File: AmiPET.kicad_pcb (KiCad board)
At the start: 2 copper layers, 68.6 x 53.3 mm, 11 parts, among them J1 Power, J2 Digital/PWM, J3 Analog, J4 Digital/PWM, J6 PET Keyboard Connector, J7 AMIGA Keyboard Connector, U1 M3493B2

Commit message: PCB Project update
tweaked layout
new 3d models
added schematic, production files, bom and image
removed old painted schematic
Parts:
- added C1: C, Capacitor_THT:C_Disc_D6.0mm_W2.5mm_P5.00mm, F.Cu at (81.6, 52.1)
- J1, J4: footprint Connector_PinSocket_2.54mm:PinSocket_1x08_P2.54mm_Vertical -> AmiPet_lib_fp:PinSocket_1x08_P2.54mm_Vertical
- J2: footprint Connector_PinSocket_2.54mm:PinSocket_1x10_P2.54mm_Vertical -> AmiPet_lib_fp:PinSocket_1x10_P2.54mm_Vertical
- J3: footprint Connector_PinSocket_2.54mm:PinSocket_1x06_P2.54mm_Vertical -> AmiPet_lib_fp:PinSocket_1x06_P2.54mm_Vertical
- MH1, MH2, MH3, MH4: footprint Arduino_MountingHole:MountingHole_3.2mm -> AmiPet_lib_fp:MountingHole_3.2mm
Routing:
- net VCC: track 84.9 -> 82.9 mm
- net /Y0: track 40.5 -> 39.2 mm
- net /KCLK: track 48.7 -> 47.6 mm, vias 2 -> 0
- net /X7: track 24.5 -> 23.8 mm
- net /AY2: track 55.5 -> 56.1 mm
- net /Y3: track 14.0 -> 13.3 mm
- net /X9: track 24.5 -> 23.8 mm
- net /X8: track 24.5 -> 23.8 mm
- net /X6: track 24.5 -> 23.8 mm
- net /AX3: track 58.6 -> 57.9 mm
- net /KDAT: track 56.4 -> 56.3 mm, vias 2 -> 0
- net GND: vias 8 -> 6
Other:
- outline, holes or cut-outs redrawn
- board text added: "CLK"
- board text added: "DAT"
- board text added: "M3493B2"
- board text added: "X3"
- board text added: "_{AMI}"
- board text removed: "C3"
- board text removed: "KCLK"
- board text removed: "KDAT"
- board text removed: "_{AMI}PET"

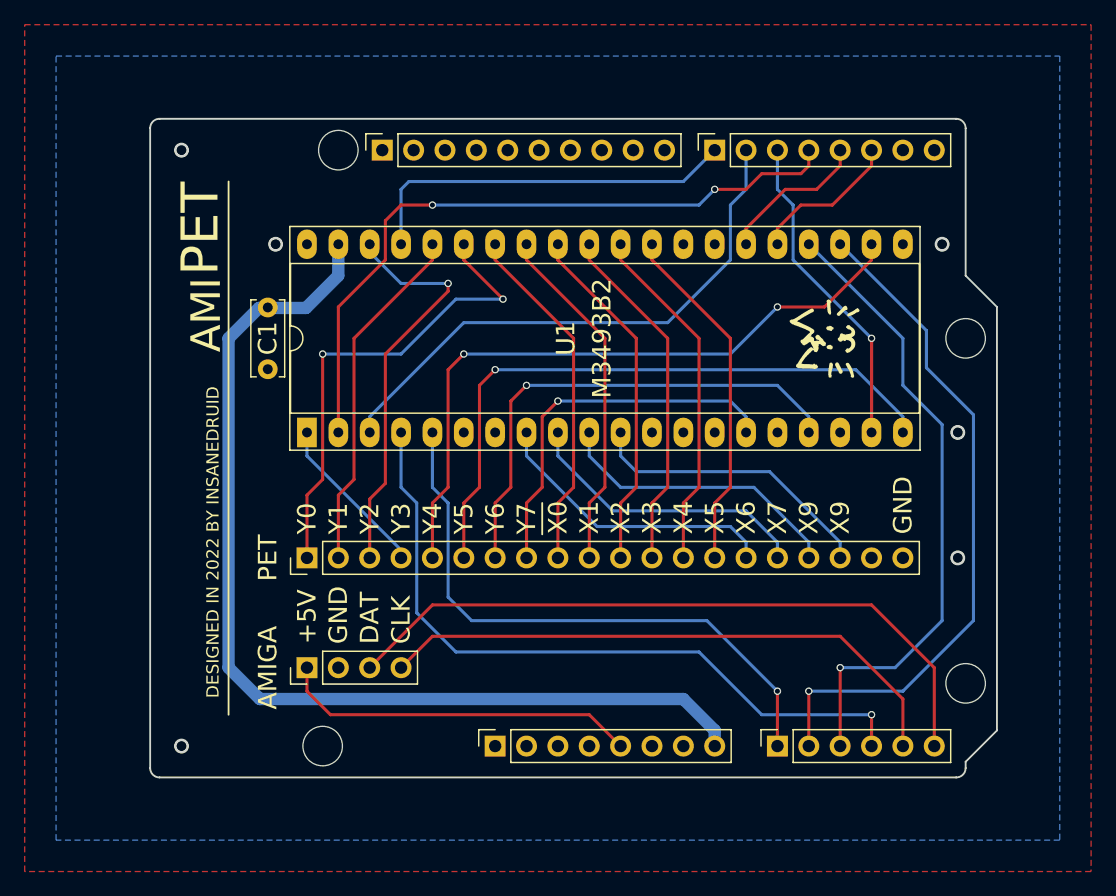
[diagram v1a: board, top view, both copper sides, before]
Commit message: added jlc order number markers
added jlc order number position marker to pcb
fixed licence links in drawing sheets to match board prints, readme and project
added desktop ini to gitignore
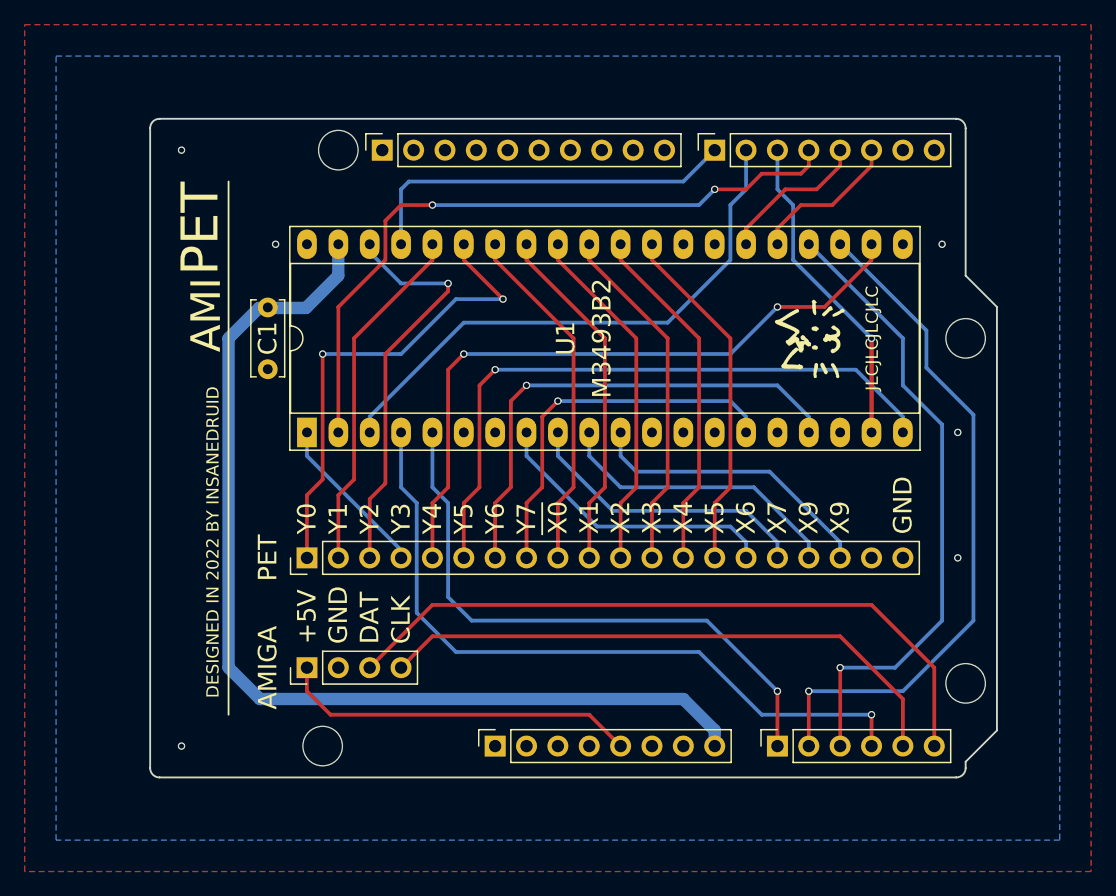
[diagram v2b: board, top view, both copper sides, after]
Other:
- board text added: "JLCJLCJLCJLC"
